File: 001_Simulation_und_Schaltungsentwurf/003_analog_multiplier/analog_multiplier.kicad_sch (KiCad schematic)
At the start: 54 parts, among them IC1 MPY634KP, IC2 MPY634KP, IC3 MPY634KP, IC4 MPY634KP, IC5 MPY634KP, IC6 MPY634KP, IC7 MPY634KP, IC8 MPY634KP, IC9 MPY634KP, U1 TL082, U2 TL082, U3 TL082, U4 TL082, U5 TL082, U6 TL082

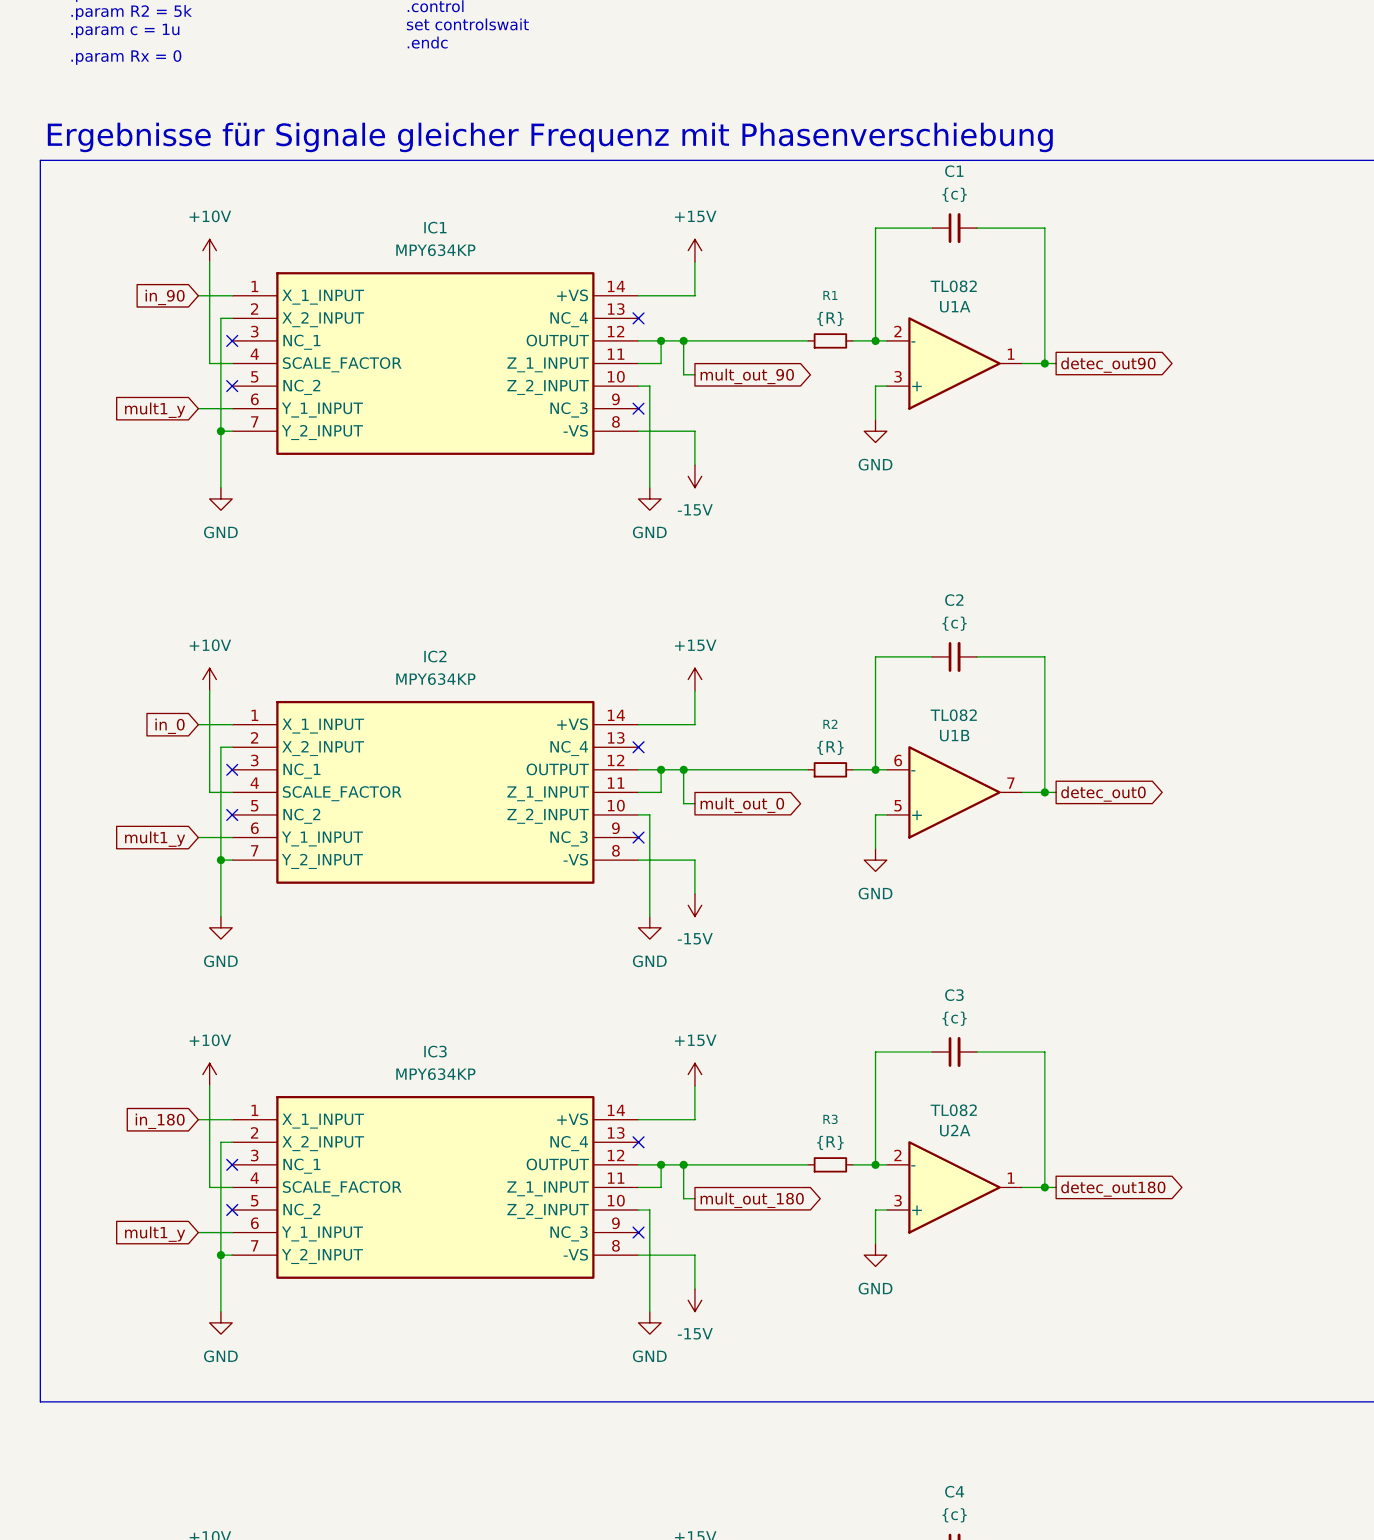
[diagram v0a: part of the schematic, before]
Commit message: PD-Vermessung und Sprungantwortsimulation
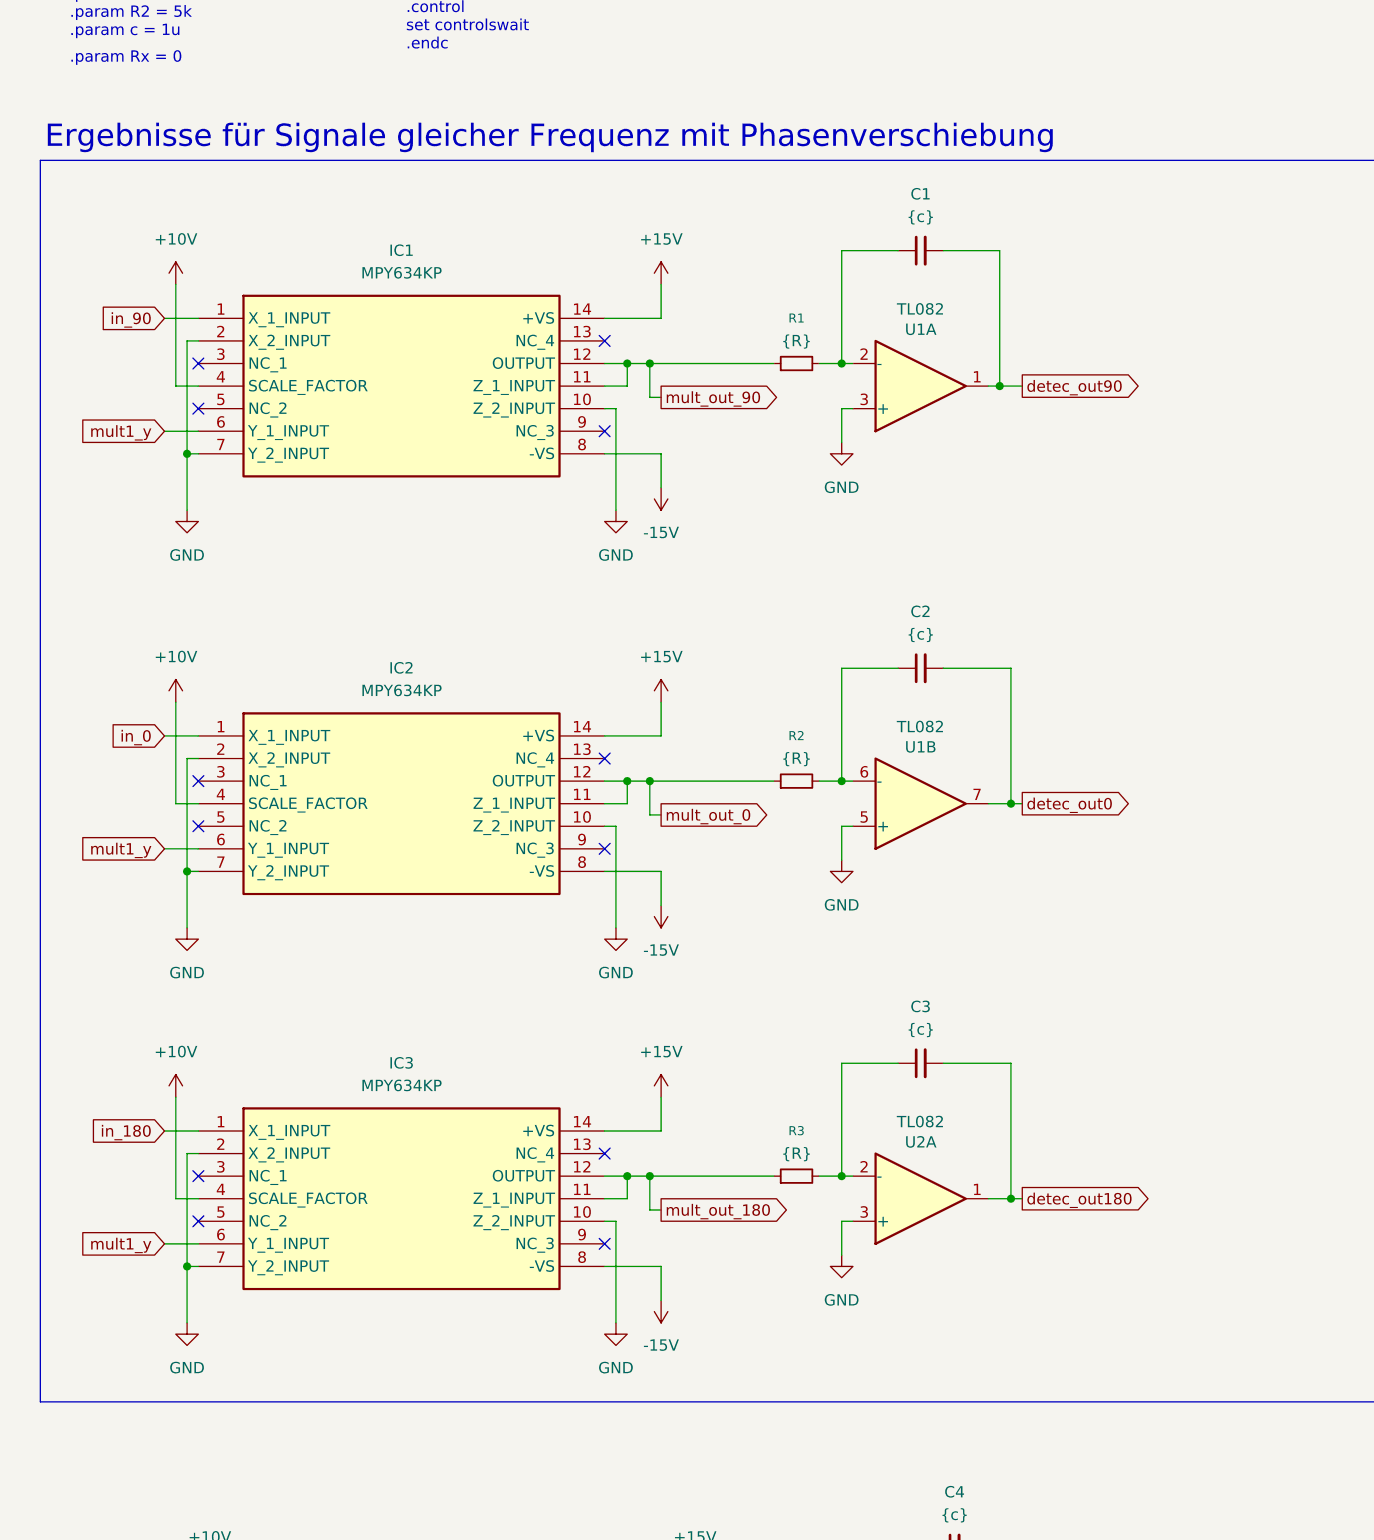
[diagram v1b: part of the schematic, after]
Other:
- moved on the sheet: C1, C2, C3, IC1, IC2, IC3, R1, R2, R3, U1A, U1B, U2A
